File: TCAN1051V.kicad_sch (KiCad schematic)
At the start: 8 parts, among them U8 TCAN1051VDRBRQ1

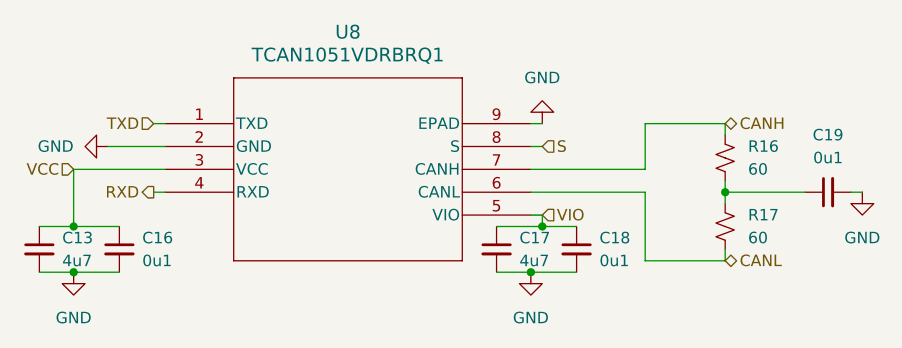
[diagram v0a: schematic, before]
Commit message: OBC: initial schematic entry complete
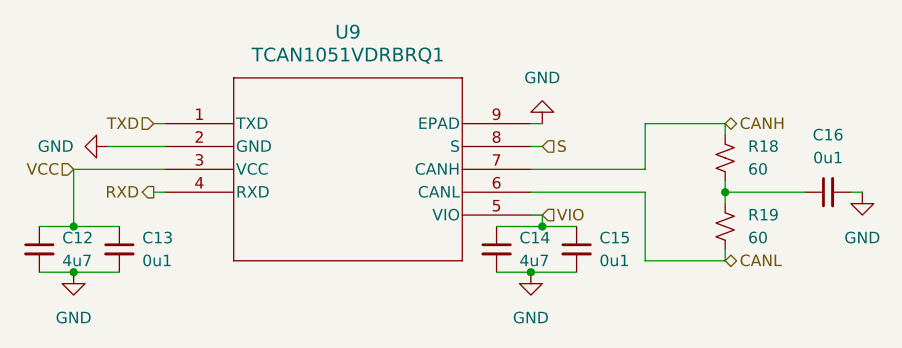
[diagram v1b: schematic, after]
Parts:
- C12: renamed from C13; footprint (none) -> Capacitor_SMD:C_0805_2012Metric
- C13: renamed from C16; footprint (none) -> Capacitor_SMD:C_0805_2012Metric
- C14: renamed from C17; footprint (none) -> Capacitor_SMD:C_0805_2012Metric
- C15: renamed from C18; footprint (none) -> Capacitor_SMD:C_0805_2012Metric
- C16: renamed from C19; footprint (none) -> Capacitor_SMD:C_0805_2012Metric
- R18: renamed from R16; footprint (none) -> Resistor_SMD:R_0805_2012Metric
- R19: renamed from R17; footprint (none) -> Resistor_SMD:R_0805_2012Metric
- renumbered U8 to U9
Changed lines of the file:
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@@
 		(dnp no)
 		(fields_autoplaced yes)
-		(property "Reference" "#PWR065"
+		(property "Reference" "#PWR088"
 			(at 226.06 118.11 0)
 			(effects
@@
 			(project "Avionics"
 				(path "/ace5002f-3cbc-4a0a-869b-0e31ebd905b7/893aef5a-59ff-410b-9a71-9930aaf04e9f/229fa22d-4bc3-493d-aaa3-1dd638eefa78"
-					(reference "#PWR065")
+					(reference "#PWR088")
+					(unit 1)
+				)
+				(path "/ace5002f-3cbc-4a0a-869b-0e31ebd905b7/893aef5a-59ff-410b-9a71-9930aaf04e9f/d3868309-a946-47d2-bb65-3f159979e5fb"
+					(reference "#PWR095")
 					(unit 1)
 				)
@@
 		(dnp no)
 		(fields_autoplaced yes)
-		(property "Reference" "#PWR012"
+		(property "Reference" "#PWR086"
 			(at 171.45 127 0)
 			(effects
@@
 			(project "Avionics"
 				(path "/ace5002f-3cbc-4a0a-869b-0e31ebd905b7/893aef5a-59ff-410b-9a71-9930aaf04e9f/229fa22d-4bc3-493d-aaa3-1dd638eefa78"
-					(reference "#PWR012")
+					(reference "#PWR086")
+					(unit 1)
+				)
+				(path "/ace5002f-3cbc-4a0a-869b-0e31ebd905b7/893aef5a-59ff-410b-9a71-9930aaf04e9f/d3868309-a946-47d2-bb65-3f159979e5fb"
+					(reference "#PWR093")
 					(unit 1)
 				)
@@
 		(dnp no)
 		(fields_autoplaced yes)
-		(property "Reference" "C18"
+		(property "Reference" "C15"
 			(at 232.41 137.1662 0)
 			(effects
@@
 			)
 		)
-		(property "Footprint" ""
+		(property "Footprint" "Capacitor_SMD:C_0805_2012Metric"
 			(at 229.87 138.43 0)
 			(effects
@@
 			(project "Avionics"
 				(path "/ace5002f-3cbc-4a0a-869b-0e31ebd905b7/893aef5a-59ff-410b-9a71-9930aaf04e9f/229fa22d-4bc3-493d-aaa3-1dd638eefa78"
-					(reference "C18")
-					(unit 1)
-				)
-				(path "/ace5002f-3cbc-4a0a-869b-0e31ebd905b7/893aef5a-59ff-410b-9a71-9930aaf04e9f/d3868309-a946-47d2-bb65-3f159979e5fb"
 					(reference "C15")
+					(unit 1)
+				)
+				(path "/ace5002f-3cbc-4a0a-869b-0e31ebd905b7/893aef5a-59ff-410b-9a71-9930aaf04e9f/d3868309-a946-47d2-bb65-3f159979e5fb"
+					(reference "C21")
 					(unit 1)
 				)
@@
 		(dnp no)
 		(fields_autoplaced yes)
-		(property "Reference" "C17"
+		(property "Reference" "C14"
 			(at 223.52 137.1662 0)
 			(effects
@@
 			)
 		)
-		(property "Footprint" ""
+		(property "Footprint" "Capacitor_SMD:C_0805_2012Metric"
 			(at 220.98 138.43 0)
 			(effects
@@
 			(project "Avionics"
 				(path "/ace5002f-3cbc-4a0a-869b-0e31ebd905b7/893aef5a-59ff-410b-9a71-9930aaf04e9f/229fa22d-4bc3-493d-aaa3-1dd638eefa78"
-					(reference "C17")
-					(unit 1)
-				)
-				(path "/ace5002f-3cbc-4a0a-869b-0e31ebd905b7/893aef5a-59ff-410b-9a71-9930aaf04e9f/d3868309-a946-47d2-bb65-3f159979e5fb"
 					(reference "C14")
+					(unit 1)
+				)
+				(path "/ace5002f-3cbc-4a0a-869b-0e31ebd905b7/893aef5a-59ff-410b-9a71-9930aaf04e9f/d3868309-a946-47d2-bb65-3f159979e5fb"
+					(reference "C20")
 					(unit 1)
 				)
@@
 		(dnp no)
 		(fields_autoplaced yes)
-		(property "Reference" "R16"
+		(property "Reference" "R18"
 			(at 248.92 126.9999 0)
 			(effects
@@
 			)
 		)
-		(property "Footprint" ""
+		(property "Footprint" "Resistor_SMD:R_0805_2012Metric"
 			(at 246.38 128.27 0)
 			(effects
@@
 			(project "Avionics"
 				(path "/ace5002f-3cbc-4a0a-869b-0e31ebd905b7/893aef5a-59ff-410b-9a71-9930aaf04e9f/229fa22d-4bc3-493d-aaa3-1dd638eefa78"
-					(reference "R16")
+					(reference "R18")
+					(unit 1)
+				)
+				(path "/ace5002f-3cbc-4a0a-869b-0e31ebd905b7/893aef5a-59ff-410b-9a71-9930aaf04e9f/d3868309-a946-47d2-bb65-3f159979e5fb"
+					(reference "R20")
 					(unit 1)
 				)
@@
 		(dnp no)
 		(fields_autoplaced yes)
-		(property "Reference" "#PWR09"
+		(property "Reference" "#PWR085"
 			(at 173.99 147.32 0)
 			(effects
@@
 			(project "Avionics"
 				(path "/ace5002f-3cbc-4a0a-869b-0e31ebd905b7/893aef5a-59ff-410b-9a71-9930aaf04e9f/229fa22d-4bc3-493d-aaa3-1dd638eefa78"
-					(reference "#PWR09")
-					(unit 1)
-				)
-				(path "/ace5002f-3cbc-4a0a-869b-0e31ebd905b7/893aef5a-59ff-410b-9a71-9930aaf04e9f/d3868309-a946-47d2-bb65-3f159979e5fb"
-					(reference "#PWR061")
+					(reference "#PWR085")
+					(unit 1)
+				)
+				(path "/ace5002f-3cbc-4a0a-869b-0e31ebd905b7/893aef5a-59ff-410b-9a71-9930aaf04e9f/d3868309-a946-47d2-bb65-3f159979e5fb"
+					(reference "#PWR092")
 					(unit 1)
 				)
@@
 		(dnp no)
 		(fields_autoplaced yes)
-		(property "Reference" "#PWR066"
+		(property "Reference" "#PWR089"
 			(at 261.62 138.43 0)
 			(effects
@@
 			(project "Avionics"
 				(path "/ace5002f-3cbc-4a0a-869b-0e31ebd905b7/893aef5a-59ff-410b-9a71-9930aaf04e9f/229fa22d-4bc3-493d-aaa3-1dd638eefa78"
-					(reference "#PWR066")
+					(reference "#PWR089")
+					(unit 1)
+				)
+				(path "/ace5002f-3cbc-4a0a-869b-0e31ebd905b7/893aef5a-59ff-410b-9a71-9930aaf04e9f/d3868309-a946-47d2-bb65-3f159979e5fb"
+					(reference "#PWR096")
 					(unit 1)
 				)
@@
 		(dnp no)
 		(fields_autoplaced yes)
-		(property "Reference" "C19"
+		(property "Reference" "C16"
 			(at 257.8163 125.73 90)
 			(effects
@@
 			)
 		)
-		(property "Footprint" ""
+		(property "Footprint" "Capacitor_SMD:C_0805_2012Metric"
 			(at 257.81 132.08 0)
 			(effects
@@
 			(project "Avionics"
 				(path "/ace5002f-3cbc-4a0a-869b-0e31ebd905b7/893aef5a-59ff-410b-9a71-9930aaf04e9f/229fa22d-4bc3-493d-aaa3-1dd638eefa78"
-					(reference "C19")
+					(reference "C16")
+					(unit 1)
+				)
+				(path "/ace5002f-3cbc-4a0a-869b-0e31ebd905b7/893aef5a-59ff-410b-9a71-9930aaf04e9f/d3868309-a946-47d2-bb65-3f159979e5fb"
+					(reference "C22")
 					(unit 1)
 				)
@@
 		(dnp no)
 		(fields_autoplaced yes)
-		(property "Reference" "U8"
+		(property "Reference" "U9"
 			(at 204.47 114.3 0)
 			(effects
@@
 			(project "Avionics"
 				(path "/ace5002f-3cbc-4a0a-869b-0e31ebd905b7/893aef5a-59ff-410b-9a71-9930aaf04e9f/229fa22d-4bc3-493d-aaa3-1dd638eefa78"
-					(reference "U8")
-					(unit 1)
-				)
-				(path "/ace5002f-3cbc-4a0a-869b-0e31ebd905b7/893aef5a-59ff-410b-9a71-9930aaf04e9f/d3868309-a946-47d2-bb65-3f159979e5fb"
-					(reference "U2")
+					(reference "U9")
+					(unit 1)
+				)
+				(path "/ace5002f-3cbc-4a0a-869b-0e31ebd905b7/893aef5a-59ff-410b-9a71-9930aaf04e9f/d3868309-a946-47d2-bb65-3f159979e5fb"
+					(reference "U11")
 					(unit 1)
 				)
@@
 		(dnp no)
 		(fields_autoplaced yes)
-		(property "Reference" "C13"
+		(property "Reference" "C12"
 			(at 172.72 137.1662 0)
 			(effects
@@
 			)
 		)
-		(property "Footprint" ""
+		(property "Footprint" "Capacitor_SMD:C_0805_2012Metric"
 			(at 170.18 138.43 0)
 			(effects
@@
 			(project "Avionics"
 				(path "/ace5002f-3cbc-4a0a-869b-0e31ebd905b7/893aef5a-59ff-410b-9a71-9930aaf04e9f/229fa22d-4bc3-493d-aaa3-1dd638eefa78"
-					(reference "C13")
+					(reference "C12")
+					(unit 1)
+				)
+				(path "/ace5002f-3cbc-4a0a-869b-0e31ebd905b7/893aef5a-59ff-410b-9a71-9930aaf04e9f/d3868309-a946-47d2-bb65-3f159979e5fb"
+					(reference "C18")
 					(unit 1)
 				)
@@
 		(dnp no)
 		(fields_autoplaced yes)
-		(property "Reference" "R17"
+		(property "Reference" "R19"
 			(at 248.92 134.6199 0)
 			(effects
@@
 			)
 		)
-		(property "Footprint" ""
+		(property "Footprint" "Resistor_SMD:R_0805_2012Metric"
 			(at 246.38 135.89 0)
 			(effects
@@
 			(project "Avionics"
 				(path "/ace5002f-3cbc-4a0a-869b-0e31ebd905b7/893aef5a-59ff-410b-9a71-9930aaf04e9f/229fa22d-4bc3-493d-aaa3-1dd638eefa78"
-					(reference "R17")
+					(reference "R19")
+					(unit 1)
+				)
+				(path "/ace5002f-3cbc-4a0a-869b-0e31ebd905b7/893aef5a-59ff-410b-9a71-9930aaf04e9f/d3868309-a946-47d2-bb65-3f159979e5fb"
+					(reference "R21")
 					(unit 1)
 				)
@@
 		(dnp no)
 		(fields_autoplaced yes)
-		(property "Reference" "C16"
+		(property "Reference" "C13"
 			(at 181.61 137.1662 0)
 			(effects
@@
 			)
 		)
-		(property "Footprint" ""
+		(property "Footprint" "Capacitor_SMD:C_0805_2012Metric"
 			(at 179.07 138.43 0)
 			(effects
@@
 			(project "Avionics"
 				(path "/ace5002f-3cbc-4a0a-869b-0e31ebd905b7/893aef5a-59ff-410b-9a71-9930aaf04e9f/229fa22d-4bc3-493d-aaa3-1dd638eefa78"
-					(reference "C16")
+					(reference "C13")
+					(unit 1)
+				)
+				(path "/ace5002f-3cbc-4a0a-869b-0e31ebd905b7/893aef5a-59ff-410b-9a71-9930aaf04e9f/d3868309-a946-47d2-bb65-3f159979e5fb"
+					(reference "C19")
 					(unit 1)
 				)
@@
 		(dnp no)
 		(fields_autoplaced yes)
-		(property "Reference" "#PWR064"
+		(property "Reference" "#PWR087"
 			(at 224.79 147.32 0)
 			(effects
@@
 			(project "Avionics"
 				(path "/ace5002f-3cbc-4a0a-869b-0e31ebd905b7/893aef5a-59ff-410b-9a71-9930aaf04e9f/229fa22d-4bc3-493d-aaa3-1dd638eefa78"
-					(reference "#PWR064")
-					(unit 1)
-				)
-				(path "/ace5002f-3cbc-4a0a-869b-0e31ebd905b7/893aef5a-59ff-410b-9a71-9930aaf04e9f/d3868309-a946-47d2-bb65-3f159979e5fb"
-					(reference "#PWR062")
-					(unit 1)
-				)
+					(reference "#PWR087")
+					(unit 1)
+				)
+				(path "/ace5002f-3cbc-4a0a-869b-0e31ebd905b7/893aef5a-59ff-410b-9a71-9930aaf04e9f/d3868309-a946-47d2-bb65-3f159979e5fb"
+					(reference "#PWR094")
+					(unit 1)
+				)

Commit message: OBC: preliminary layout
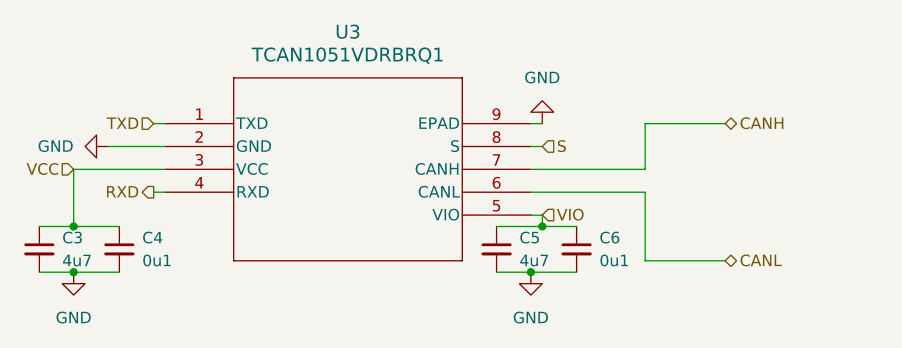
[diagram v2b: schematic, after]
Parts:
- removed C16: 0u1, Capacitor_SMD:C_0805_2012Metric, symbol Device:C_Small
- removed R18, R19: 60, Resistor_SMD:R_0805_2012Metric, symbol Device:R_Small_US
- U3: renamed from U9; footprint DRB8_TEX -> TCAN1051V:DRB8_TEX
- renumbered C12 to C3, C13 to C4, C14 to C5, C15 to C6

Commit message: OBC: start PCB layout
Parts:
- renumbered U3 to U2
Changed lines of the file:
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@@
 		(dnp no)
 		(fields_autoplaced yes)
-		(property "Reference" "#PWR044"
+		(property "Reference" "#PWR045"
 			(at 226.06 118.11 0)
 			(effects
@@
 			(project "Avionics"
 				(path "/ace5002f-3cbc-4a0a-869b-0e31ebd905b7/893aef5a-59ff-410b-9a71-9930aaf04e9f/229fa22d-4bc3-493d-aaa3-1dd638eefa78"
-					(reference "#PWR044")
-					(unit 1)
-				)
-				(path "/ace5002f-3cbc-4a0a-869b-0e31ebd905b7/893aef5a-59ff-410b-9a71-9930aaf04e9f/d3868309-a946-47d2-bb65-3f159979e5fb"
-					(reference "#PWR050")
+					(reference "#PWR045")
+					(unit 1)
+				)
+				(path "/ace5002f-3cbc-4a0a-869b-0e31ebd905b7/893aef5a-59ff-410b-9a71-9930aaf04e9f/d3868309-a946-47d2-bb65-3f159979e5fb"
+					(reference "#PWR051")
 					(unit 1)
 				)
@@
 		(dnp no)
 		(fields_autoplaced yes)
-		(property "Reference" "#PWR042"
+		(property "Reference" "#PWR043"
 			(at 171.45 127 0)
 			(effects
@@
 			(project "Avionics"
 				(path "/ace5002f-3cbc-4a0a-869b-0e31ebd905b7/893aef5a-59ff-410b-9a71-9930aaf04e9f/229fa22d-4bc3-493d-aaa3-1dd638eefa78"
-					(reference "#PWR042")
-					(unit 1)
-				)
-				(path "/ace5002f-3cbc-4a0a-869b-0e31ebd905b7/893aef5a-59ff-410b-9a71-9930aaf04e9f/d3868309-a946-47d2-bb65-3f159979e5fb"
-					(reference "#PWR048")
+					(reference "#PWR043")
+					(unit 1)
+				)
+				(path "/ace5002f-3cbc-4a0a-869b-0e31ebd905b7/893aef5a-59ff-410b-9a71-9930aaf04e9f/d3868309-a946-47d2-bb65-3f159979e5fb"
+					(reference "#PWR049")
 					(unit 1)
 				)
@@
 		(dnp no)
 		(fields_autoplaced yes)
-		(property "Reference" "#PWR041"
+		(property "Reference" "#PWR042"
 			(at 173.99 147.32 0)
 			(effects
@@
 			(project "Avionics"
 				(path "/ace5002f-3cbc-4a0a-869b-0e31ebd905b7/893aef5a-59ff-410b-9a71-9930aaf04e9f/229fa22d-4bc3-493d-aaa3-1dd638eefa78"
-					(reference "#PWR041")
-					(unit 1)
-				)
-				(path "/ace5002f-3cbc-4a0a-869b-0e31ebd905b7/893aef5a-59ff-410b-9a71-9930aaf04e9f/d3868309-a946-47d2-bb65-3f159979e5fb"
-					(reference "#PWR047")
+					(reference "#PWR042")
+					(unit 1)
+				)
+				(path "/ace5002f-3cbc-4a0a-869b-0e31ebd905b7/893aef5a-59ff-410b-9a71-9930aaf04e9f/d3868309-a946-47d2-bb65-3f159979e5fb"
+					(reference "#PWR048")
 					(unit 1)
 				)
@@
 		(dnp no)
 		(fields_autoplaced yes)
-		(property "Reference" "U3"
+		(property "Reference" "U2"
 			(at 204.47 114.3 0)
 			(effects
@@
 			(project "Avionics"
 				(path "/ace5002f-3cbc-4a0a-869b-0e31ebd905b7/893aef5a-59ff-410b-9a71-9930aaf04e9f/229fa22d-4bc3-493d-aaa3-1dd638eefa78"
-					(reference "U3")
-					(unit 1)
-				)
-				(path "/ace5002f-3cbc-4a0a-869b-0e31ebd905b7/893aef5a-59ff-410b-9a71-9930aaf04e9f/d3868309-a946-47d2-bb65-3f159979e5fb"
-					(reference "U5")
+					(reference "U2")
+					(unit 1)
+				)
+				(path "/ace5002f-3cbc-4a0a-869b-0e31ebd905b7/893aef5a-59ff-410b-9a71-9930aaf04e9f/d3868309-a946-47d2-bb65-3f159979e5fb"
+					(reference "U4")
 					(unit 1)
 				)
@@
 		(dnp no)
 		(fields_autoplaced yes)
-		(property "Reference" "#PWR043"
+		(property "Reference" "#PWR044"
 			(at 224.79 147.32 0)
 			(effects
@@
 			(project "Avionics"
 				(path "/ace5002f-3cbc-4a0a-869b-0e31ebd905b7/893aef5a-59ff-410b-9a71-9930aaf04e9f/229fa22d-4bc3-493d-aaa3-1dd638eefa78"
-					(reference "#PWR043")
-					(unit 1)
-				)
-				(path "/ace5002f-3cbc-4a0a-869b-0e31ebd905b7/893aef5a-59ff-410b-9a71-9930aaf04e9f/d3868309-a946-47d2-bb65-3f159979e5fb"
-					(reference "#PWR049")
-					(unit 1)
-				)
+					(reference "#PWR044")
+					(unit 1)
+				)
+				(path "/ace5002f-3cbc-4a0a-869b-0e31ebd905b7/893aef5a-59ff-410b-9a71-9930aaf04e9f/d3868309-a946-47d2-bb65-3f159979e5fb"
+					(reference "#PWR050")
+					(unit 1)
+				)
